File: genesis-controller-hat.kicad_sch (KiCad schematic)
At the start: 6 parts, among them J1 GPIO, U1 CAT24C256

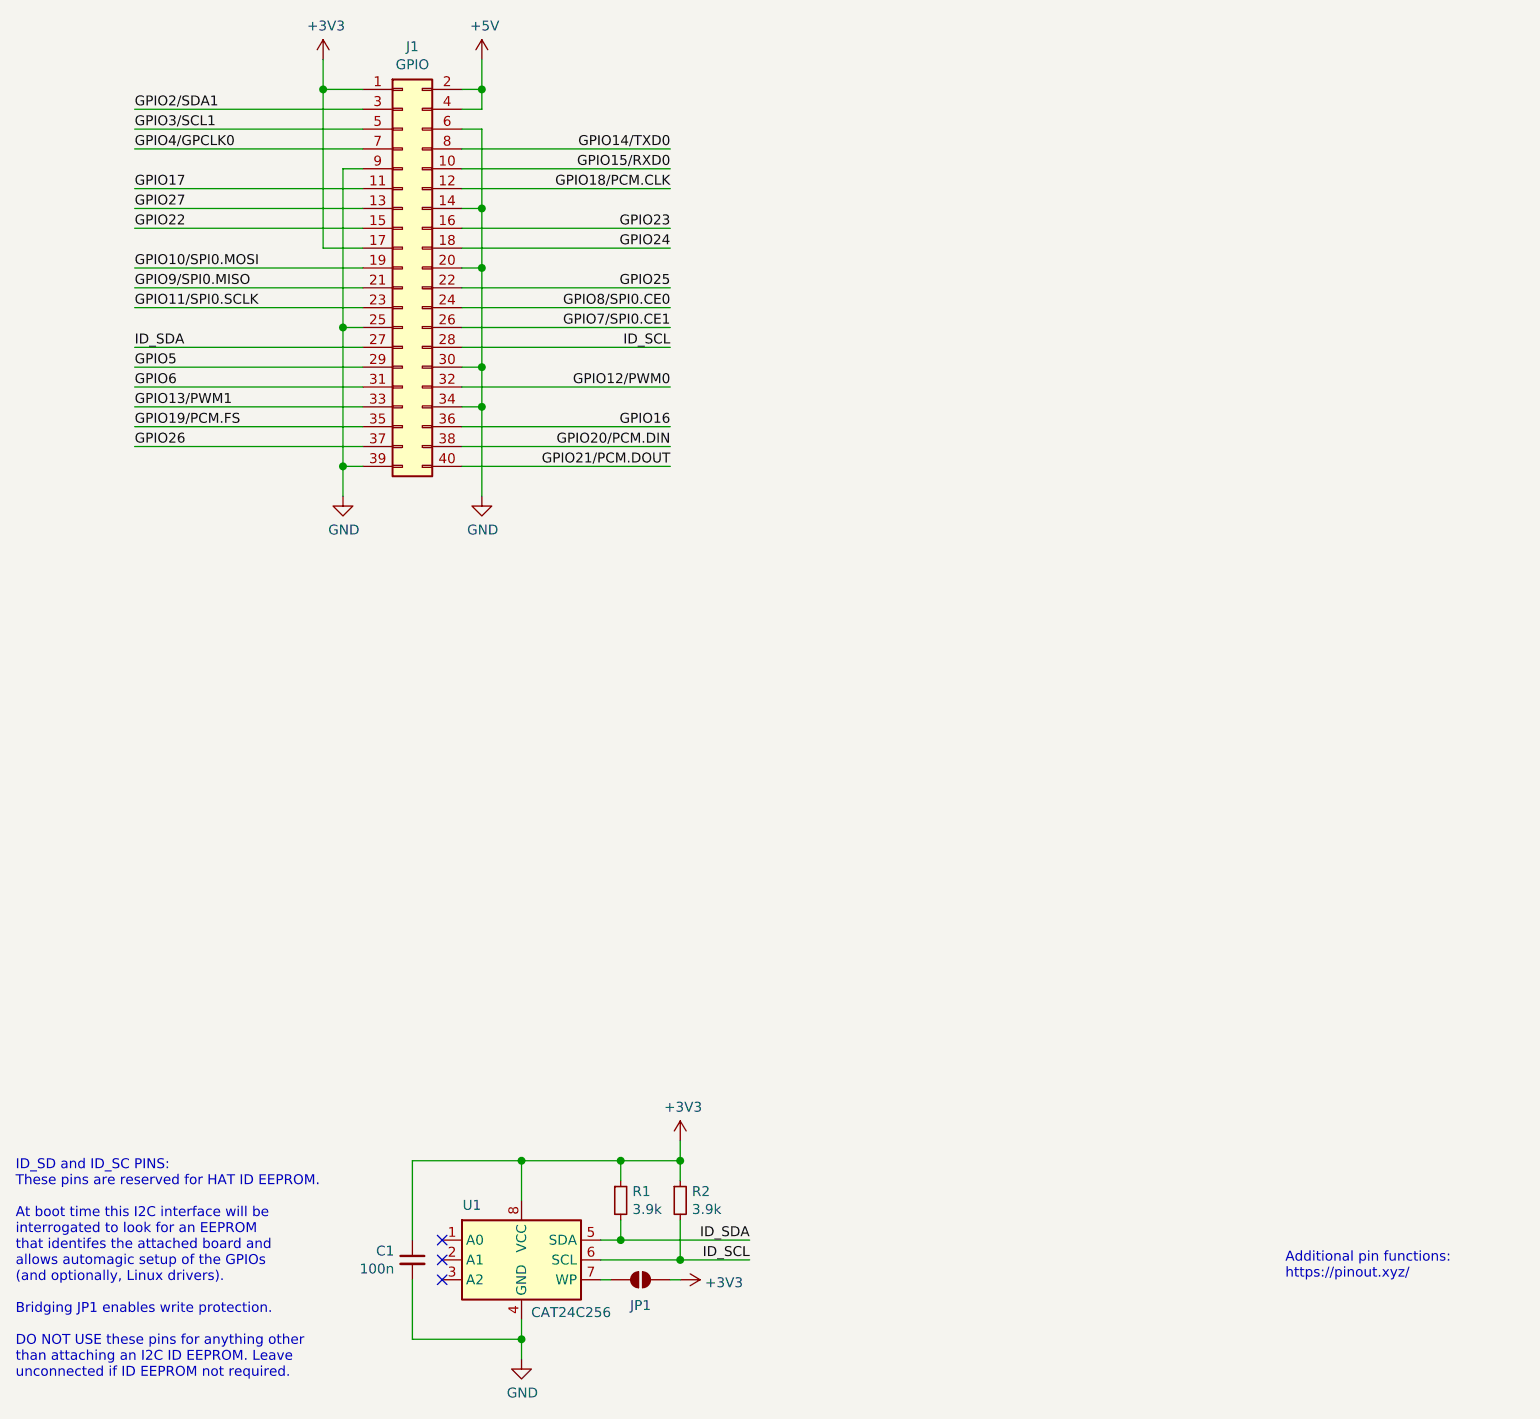
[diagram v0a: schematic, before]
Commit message: Strip ID EEPROM circuit and +5V from the HAT schematic
This board is not chasing official HAT certification (bare-metal kernel,
no device-tree consumer for the EEPROM) and never uses 5V (Genesis pads
are powered at 3.3V per the approved design spec), so both are removed
rather than left as dead weight, along with the ID_SDA/ID_SCL label pairs
and wiring that only existed to serve the EEPROM circuit. PWR_FLAG symbols
replace the ERC correctness those deleted parts incidentally provided for
the +3.3V/GND nets; GPIO0/1 get explicit no-connect flags.

Co-Authored-By: Claude Sonnet 5 <noreply@anthropic.com>
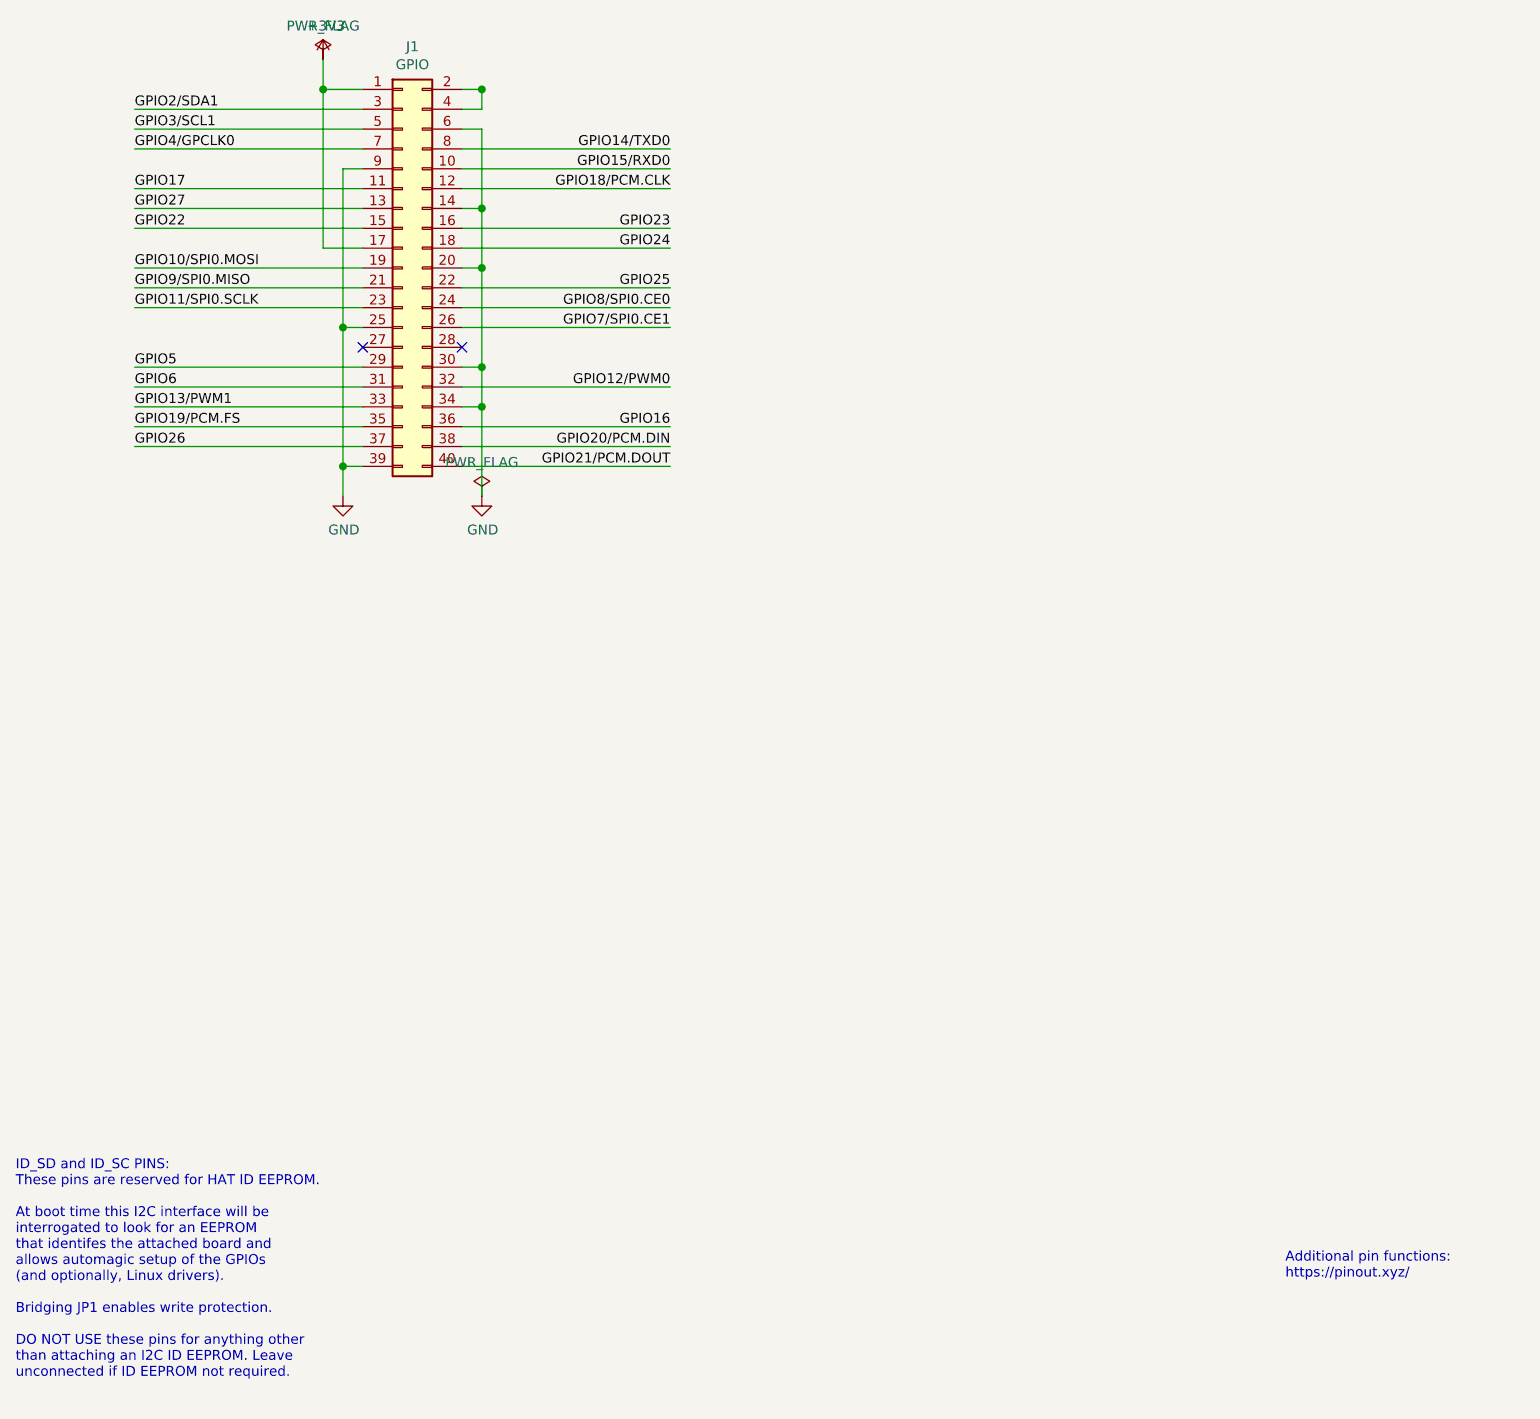
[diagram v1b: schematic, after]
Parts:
- removed C1: 100n, symbol Device:C_Small
- removed JP1: ID_WP, symbol Jumper:SolderJumper_2_Open
- removed R1, R2: 3.9k, symbol Device:R_Small
- removed U1: CAT24C256, symbol Memory_EEPROM:CAT24C256
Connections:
- net +5V: no longer names the net of J1.2 (Pin_2), J1.4 (Pin_4)
- net ID_SCL: no longer names the net of J1.28 (Pin_28)
- net ID_SDA: no longer names the net of J1.27 (Pin_27)
- no-connect marks 3 -> 2
